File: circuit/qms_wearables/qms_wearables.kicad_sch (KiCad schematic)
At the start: 5 parts, among them P1 SEN-11574, U1 ESP32-DEVKIT-V1, U2 module_mpu6050

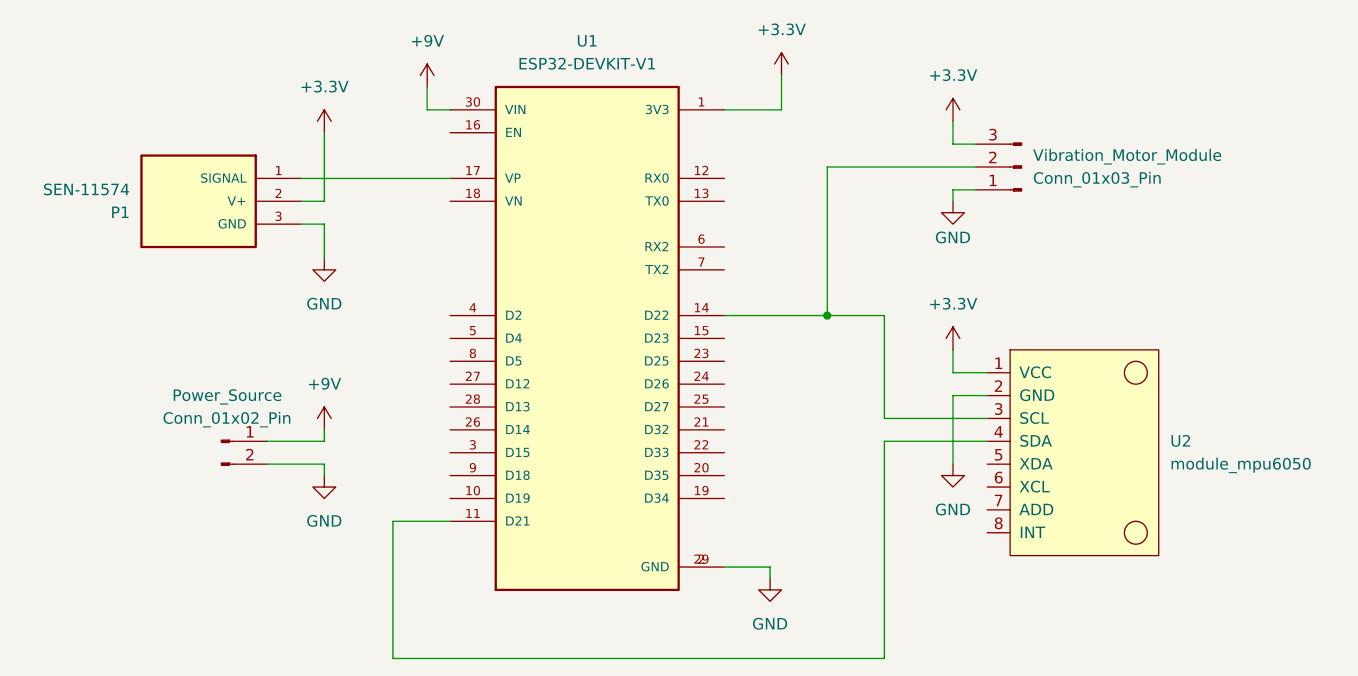
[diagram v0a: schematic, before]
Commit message: fix: wrong input voltage to ESP32
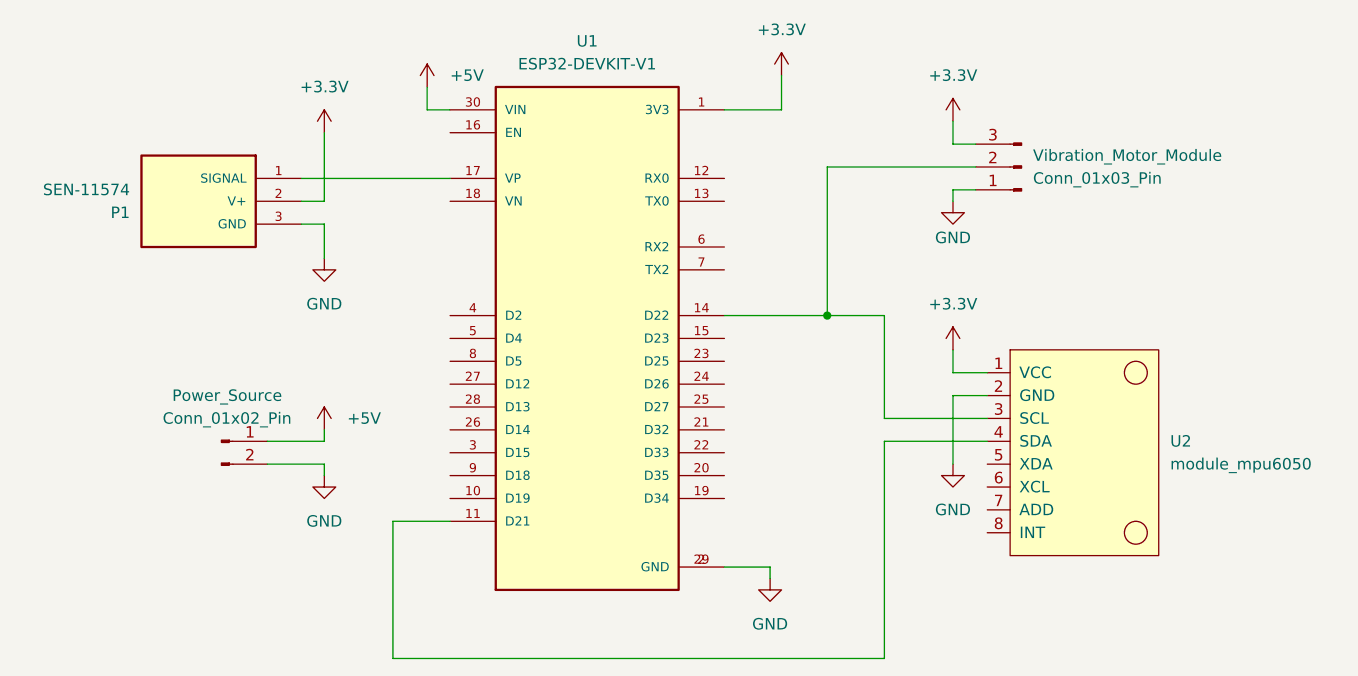
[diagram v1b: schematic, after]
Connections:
- net +9V renamed +5V
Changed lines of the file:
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@@
 			)
 		)
-		(property "Value" "+9V"
-			(at 93.98 59.69 0)
-			(effects
-				(font
-					(size 1.27 1.27)
-				)
+		(property "Value" "+5V"
+			(at 96.52 63.4999 0)
+			(effects
+				(font
+					(size 1.27 1.27)
+				)
+				(justify left)
 			)
 		)
@@
 			)
 		)
-		(property "Value" "+9V"
-			(at 82.55 97.79 0)
-			(effects
-				(font
-					(size 1.27 1.27)
-				)
-			)
-		)
+		(property "Value" "+5V"
+			(at 85.09 101.5999 0)
+			(effects
+				(font
+					(size 1.27 1.27)
+				)
+				(justify left)
+			)
+		)

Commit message: wip: Update the pcb footprint of the components in wearables circuit.
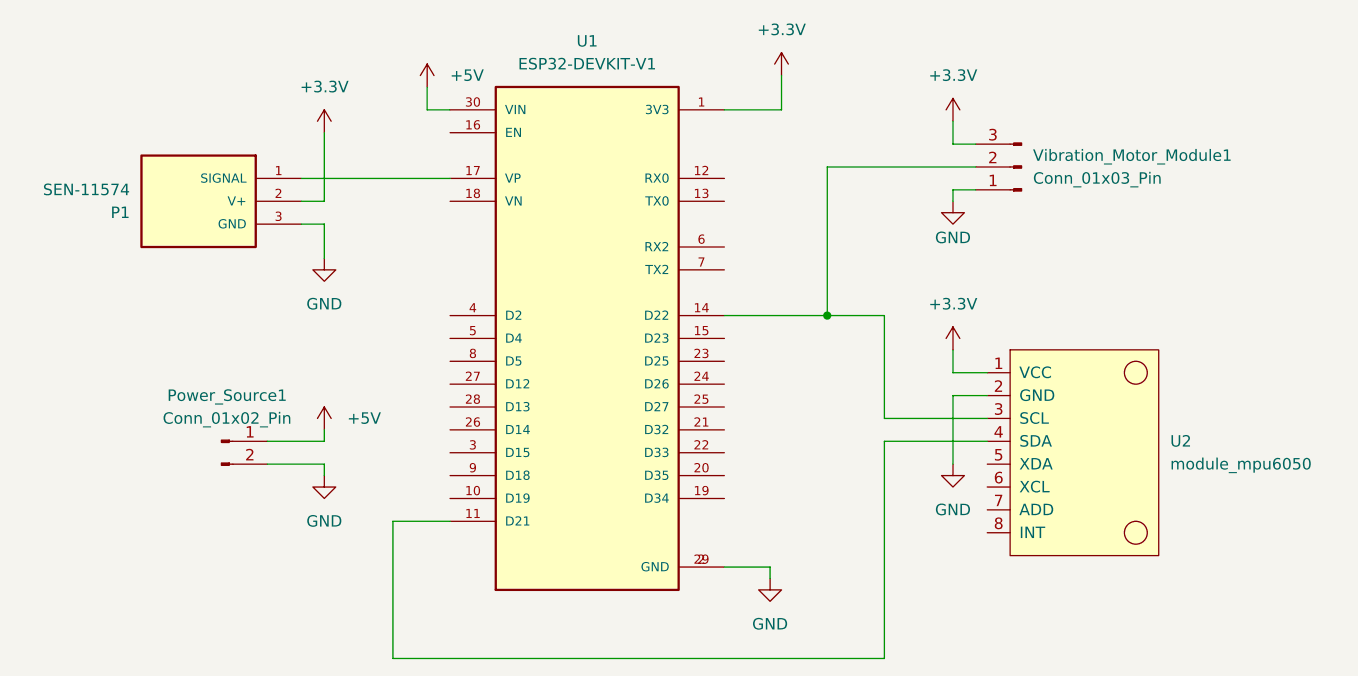
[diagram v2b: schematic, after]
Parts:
- P1: footprint SEN-11574:XDCR_SEN-11574 -> SEN_11574:XDCR_SEN-11574
- U2: footprint usini_sensors:module_mpu6050 -> MPU6050_MODULE:module_mpu6050
- renumbered Power_Source to Power_Source1, Vibration_Motor_Module to Vibration_Motor_Module1
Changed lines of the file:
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@@
 		(dnp no)
 		(fields_autoplaced yes)
-		(property "Reference" "Power_Source"
+		(property "Reference" "Power_Source1"
 			(at 71.755 99.06 0)
 			(effects
@@
 			(project ""
 				(path "/81221e85-c470-4436-ab82-7fff3486476b"
-					(reference "Power_Source")
+					(reference "Power_Source1")
 					(unit 1)
 				)
@@
 			)
 		)
-		(property "Footprint" "usini_sensors:module_mpu6050"
+		(property "Footprint" "MPU6050_MODULE:module_mpu6050"
 			(at 167.64 120.65 0)
 			(effects
@@
 		(dnp no)
 		(fields_autoplaced yes)
-		(property "Reference" "Vibration_Motor_Module"
+		(property "Reference" "Vibration_Motor_Module1"
 			(at 161.29 72.3899 0)
 			(effects
@@
 			(project ""
 				(path "/81221e85-c470-4436-ab82-7fff3486476b"
-					(reference "Vibration_Motor_Module")
+					(reference "Vibration_Motor_Module1")
 					(unit 1)
 				)
@@
 			)
 		)
-		(property "Footprint" "SEN-11574:XDCR_SEN-11574"
+		(property "Footprint" "SEN_11574:XDCR_SEN-11574"
 			(at 74.93 77.47 0)
 			(effects
